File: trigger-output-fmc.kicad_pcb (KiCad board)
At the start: 8 copper layers, 84 x 69 mm, 335 parts, among them J1 MMCX, J10 MMCX, J11 MMCX, J12 MMCX, J13 MMCX, J14 MMCX, J15 MMCX, J16 MMCX, J19 WP Jumper, J2 MMCX, J3 MMCX, J4 MMCX, J5 MMCX, J6 MMCX, J7 MMCX, J8 MMCX, J9 MMCX, P1 ASP-134488-01, Q1 FDN335N, Q2 FDN335N, Q3 FDN335N, T1 TCM2-43X+, T2 TCM2-43X+, T3 TCM2-43X+, T4 TCM2-43X+, U1 TLV3601, U10 SN74LVC2G126, U11 TLV3601, U12 SN74LVC2G126, U13 TLV3601, U14 SN74LVC2G126, U15 TLV3601, U16 SN74LVC2G126, U17 TLV3601, U18 SI5394, U19 SI5394, U2 TLV3601, U20 TLV75733PDBV, U21 TLV75718PDBV, U22 TPS563200, U23 74AVC4T245, U24 TLV75733PDBV, U25 74AVC4T245, U26 74LVC8T245, U27 74LVC8T245, U28 TLV75718PDBV, U29 SN74LVC2G126, U3 TLV3601, U30 TLV3601, U31 SN74LVC2G126, U32 TLV3601, U33 SN74LVC2G126, U34 TLV3601, U35 SN74LVC2G126, U36 TLV3601, U37 SN74LVC2G126, U38 TLV3601, U39 SN74LVC2G126, U4 SN74LVC2G126, U40 TLV3601, U41 SN74LVC2G126, U42 TLV3601, U43 SN74LVC2G126, U44 LP3855EMP-ADJ/NOPB, U48 SN74LVC2G126, U5 SN74LVC2G126, U6 TLV3601, U7 SN74LVC2G126, U8 TLV3601, U9 AT24C64D, Y1 CX3225SB48000D0FPJC1, Y2 CX3225SB48000D0FPJC1

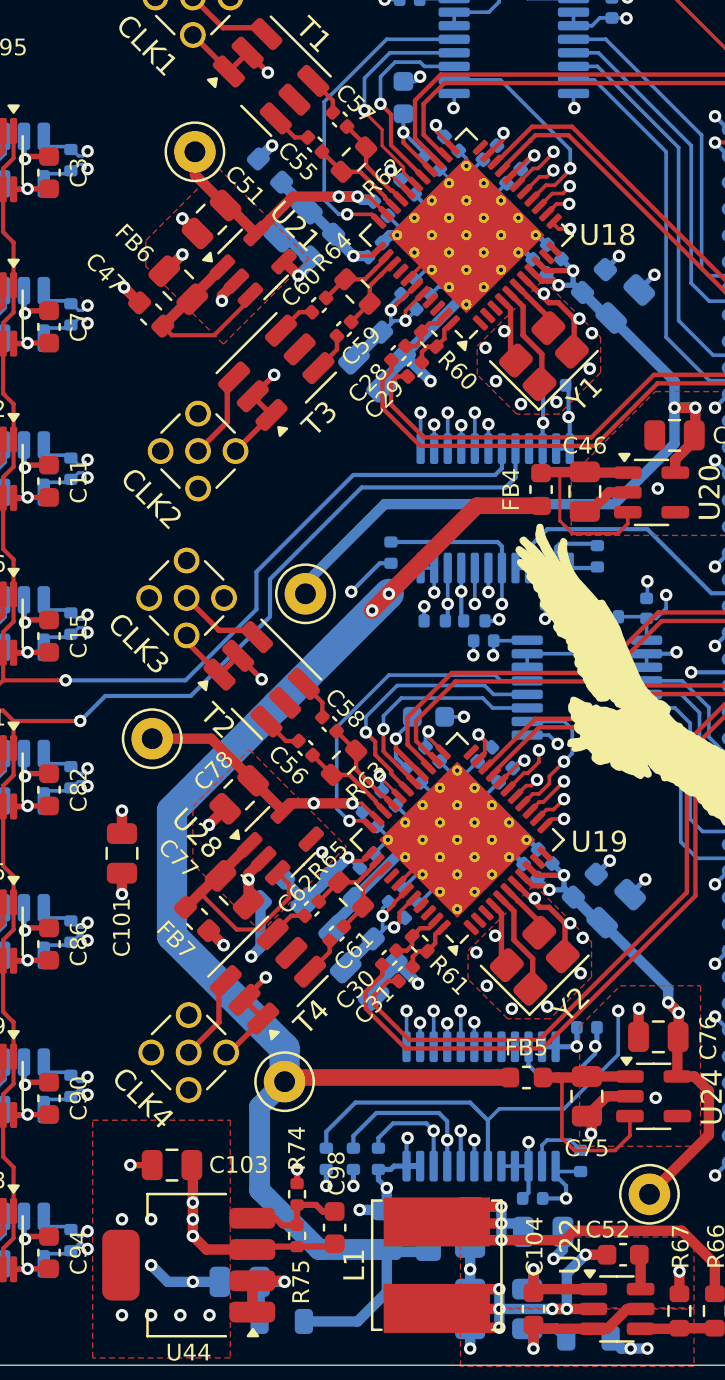
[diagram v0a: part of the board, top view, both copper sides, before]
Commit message: updated some trace widths and zone definitions
-removed all 0.3mm & 0.14mm traces.
  *Changed to other sizes
- Added a zone keepout under Y1 on In3 layer
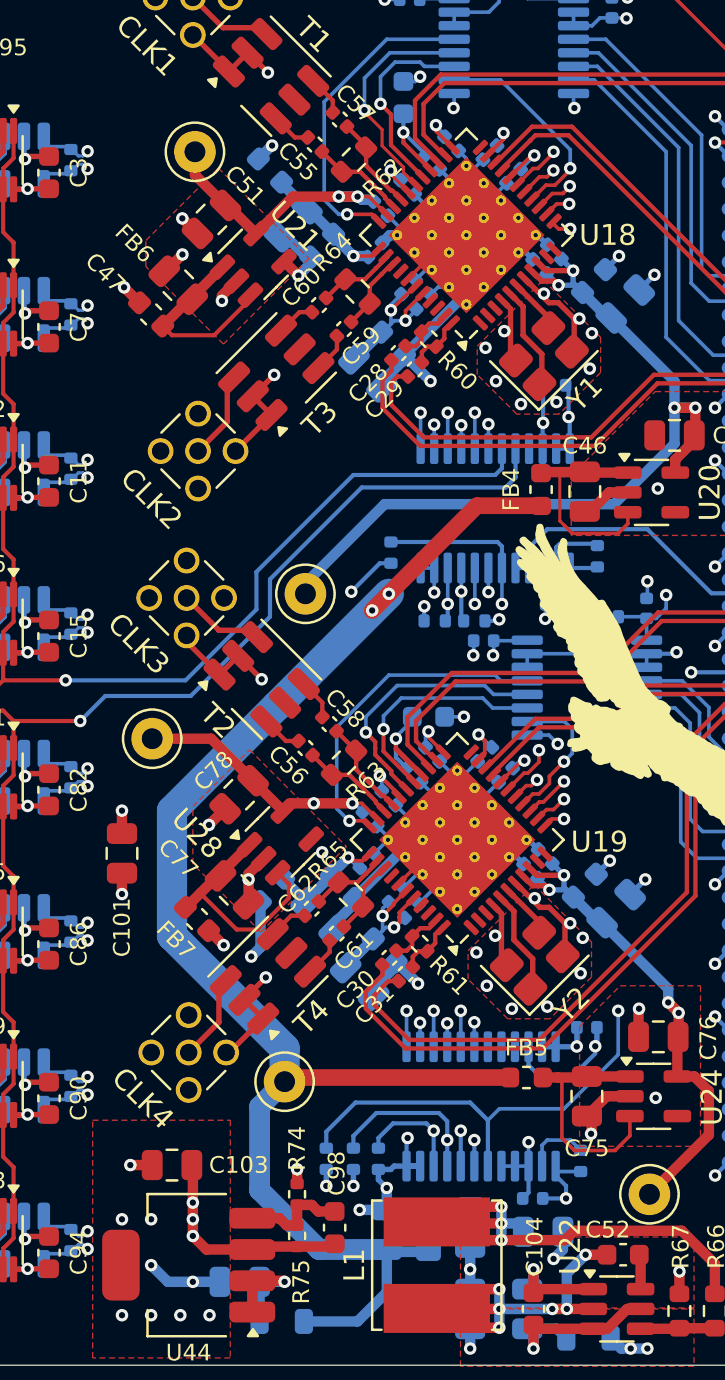
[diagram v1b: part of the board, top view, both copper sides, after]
